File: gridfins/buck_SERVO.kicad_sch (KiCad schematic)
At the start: 30 parts, among them Q1 SSM3K15AMFV,L3F, U6 SiC437AED-T1

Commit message: Power distribution rework
Added missing main power supply voltage to Stepper Motor Driver Board

Separate Buck converter for servo and linear actuator(stepper motor)

16.8V -> Buck -> high side switch -> H-bridge -> 10V
16.8V -> Buck -> Servo -> 7.4V
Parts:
- renumbered C38 to C80, C39 to C81, C40 to C82, C46 to C83, C47 to C84, C48 to C85, C49 to C86, C61 to C87, C62 to C88, C64 to C89, C65 to C90, C66 to C91, C75 to C92, C76 to C93, C77 to C94, C78 to C95, C79 to C96, L4 to L6, Q1 to Q4, R20 to R58, R21 to R59, R22 to R60, R23 to R61, R24 to R62, R38 to R63, R39 to R64, R42 to R65, R56 to R66, R57 to R67, U6 to U12
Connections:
- net +10V renamed +7.4V

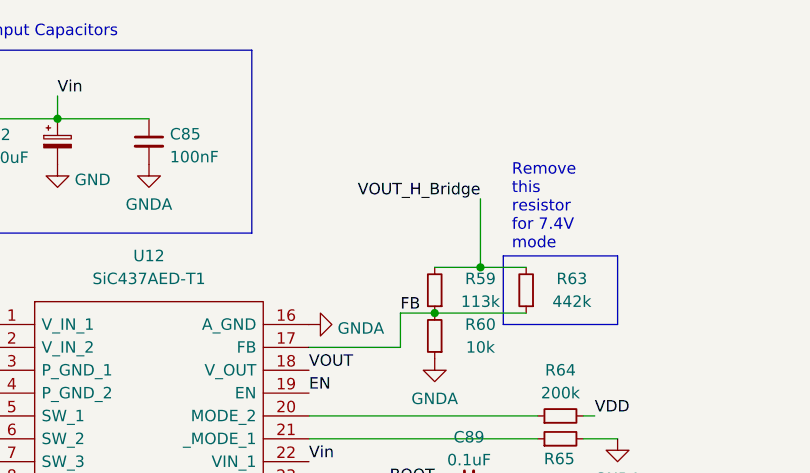
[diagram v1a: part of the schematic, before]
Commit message: PCB + schematic updates
Solved footprint error which prevented PCB from updating

Deleted old buck converter PCB design (old buck now replaced with 2 for servo and linear acc)

Moved Snubber and crossed out capacitor network to the backside of board

Unsure whether if the +10V routing is valid - currently connected via tracers, not planes (may be a problem for current)

Restructured old pcb which previously had planes associated with no nets (assigned nets to them)

If current design approved, will proceed to carry out the same design for the servo controlling buck converter.
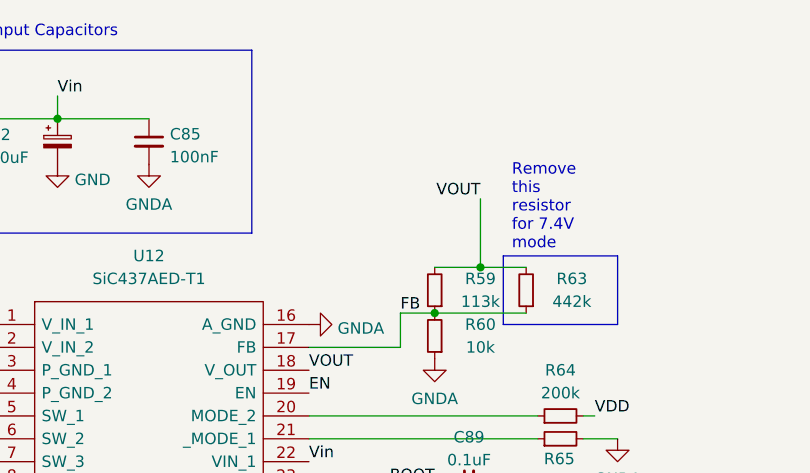
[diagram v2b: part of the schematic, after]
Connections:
- net VOUT_H_Bridge is gone; now on net +7.4V: R59.2, R63.2
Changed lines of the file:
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@@
 		)
 	)
-	(label "VOUT_H_Bridge"
+	(label "VOUT"
 		(at 121.92 52.07 180)
 		(effects
